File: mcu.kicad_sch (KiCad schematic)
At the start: 20 parts, among them J1 Conn_01x05, U1 STM32G473CCUx, Y1 8 MHz

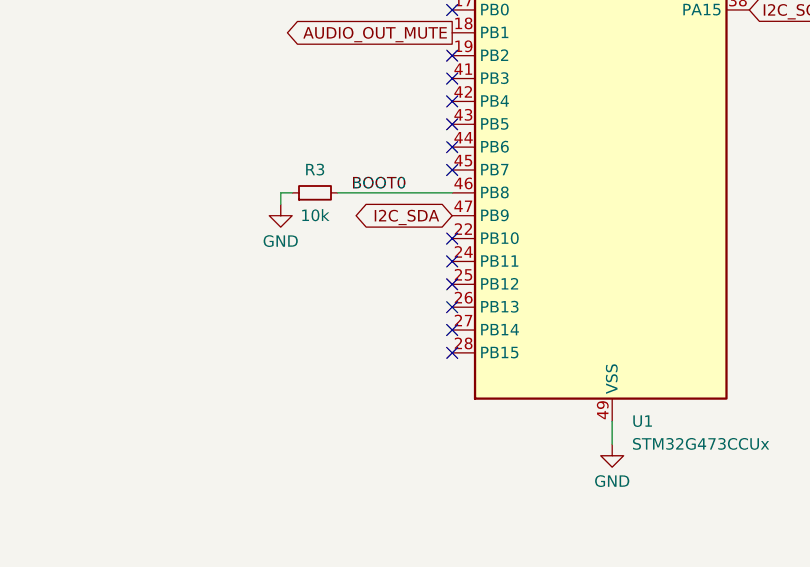
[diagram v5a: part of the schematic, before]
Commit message: J2 Corrected, More TP added.
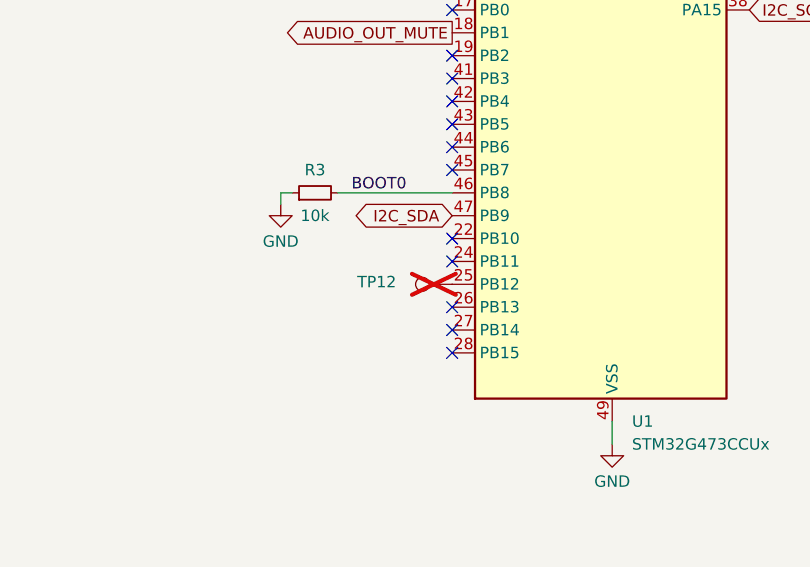
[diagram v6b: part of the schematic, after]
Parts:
- added TP12: GP, TestPoint:TestPoint_Pad_D1.0mm, symbol Connector:TestPoint
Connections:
- net at U1.25 (PB12): now also TP12.1
- no-connect marks 24 -> 23
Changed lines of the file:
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@@
+	)
+	(no_connect
+		(at 154.94 96.52)
+	)
+	(no_connect
+		(at 121.92 129.54)
+	)
+	(no_connect
+		(at 154.94 93.98)
+	)
+	(no_connect
+		(at 121.92 119.38)
+	)
+	(no_connect
+		(at 121.92 139.7)
+	)
+	(no_connect
+		(at 121.92 132.08)
+	)
+	(no_connect
+		(at 121.92 104.14)
+	)
+	(no_connect
+		(at 121.92 142.24)
+	)
+	(no_connect
+		(at 121.92 121.92)
+	)
+	(no_connect
+		(at 121.92 88.9)
+	)
+	(no_connect
+		(at 121.92 114.3)
+	)
+	(no_connect
+		(at 134.62 60.96)
+	)
+	(no_connect
+		(at 121.92 116.84)
+	)
+	(no_connect
+		(at 121.92 83.82)
+	)
+	(no_connect
+		(at 121.92 96.52)
 	)
 	(no_connect
 		(at 121.92 137.16)
-	)
-	(no_connect
-		(at 154.94 96.52)
-	)
-	(no_connect
-		(at 121.92 129.54)
-	)
-	(no_connect
-		(at 154.94 93.98)
-	)
-	(no_connect
-		(at 121.92 119.38)
-	)
-	(no_connect
-		(at 121.92 132.08)
-	)
-	(no_connect
-		(at 121.92 134.62)
-	)
-	(no_connect
-		(at 121.92 104.14)
-	)
-	(no_connect
-		(at 121.92 142.24)
-	)
-	(no_connect
-		(at 121.92 121.92)
-	)
-	(no_connect
-		(at 121.92 88.9)
-	)
-	(no_connect
-		(at 121.92 114.3)
-	)
-	(no_connect
-		(at 134.62 60.96)
-	)
-	(no_connect
-		(at 121.92 116.84)
-	)
-	(no_connect
-		(at 121.92 83.82)
-	)
-	(no_connect
-		(at 121.92 139.7)
-	)
-	(no_connect
-		(at 121.92 96.52)
 	)
 	(no_connect
@@
 					(unit 1)
 				)
+			)
+		)
+	)
+	(symbol
+		(lib_id "Connector:TestPoint")
+		(at 121.92 134.62 90)
+		(unit 1)
+		(exclude_from_sim no)
+		(in_bom no)
+		(on_board yes)
+		(dnp yes)
+		(property "Reference" "TP12"
+			(at 113.538 134.366 90)
+			(effects
+				(font
+					(size 1.27 1.27)
+				)
+			)
+		)
+		(property "Value" "GP"
+			(at 116.84 133.3501 90)
+			(effects
+				(font
+					(size 1.27 1.27)
+				)
+				(justify left)
+				(hide yes)
+			)
+		)
+		(property "Footprint" "TestPoint:TestPoint_Pad_D1.0mm"
+			(at 121.92 129.54 0)
+			(effects
+				(font
+					(size 1.27 1.27)
+				)
+				(hide yes)
+			)
+		)
+		(property "Datasheet" "~"
+			(at 121.92 129.54 0)
+			(effects
+				(font
+					(size 1.27 1.27)
+				)
+				(hide yes)
+			)
+		)
+		(property "Description" ""
+			(at 121.92 134.62 0)
+			(effects
+				(font
+					(size 1.27 1.27)
+				)
+				(hide yes)
+			)
+		)
+		(property "MPN" ""
+			(at 121.92 134.62 0)
+			(effects
+				(font
+					(size 1.27 1.27)
+				)
+				(hide yes)
+			)
+		)
+		(property "Height" ""
+			(at 121.92 134.62 0)
+			(effects
+				(font
+					(size 1.27 1.27)
+				)
+				(hide yes)
+			)
+		)
+		(property "Manufacturer_Name" ""
+			(at 121.92 134.62 0)
+			(effects
+				(font
+					(size 1.27 1.27)
+				)
+				(hide yes)
+			)
+		)
+		(property "Manufacturer_Part_Number" ""
+			(at 121.92 134.62 0)
+			(effects
+				(font
+					(size 1.27 1.27)
+				)
+				(hide yes)
+			)
+		)
+		(property "Mouser Part Number" ""
+			(at 121.92 134.62 0)
+			(effects
+				(font
+					(size 1.27 1.27)
+				)
+				(hide yes)
+			)
+		)
+		(property "Mouser Price/Stock" ""
+			(at 121.92 134.62 0)
+			(effects
+				(font
+					(size 1.27 1.27)
+				)
+				(hide yes)
+			)
+		)
+		(property "JLC" ""
+			(at 121.92 134.62 0)
+			(effects
+				(font
+					(size 1.27 1.27)
+				)
+				(hide yes)
+			)
+		)
+		(pin "1"
+		)
+		(instances
+			(project "micro17"
+				(path "/8b0d7f56-1962-40c9-8b95-6d4fe558acbc/9f9e0b5b-f07d-4ebd-b315-be375c62719d"
+					(reference "TP12")
+					(unit 1)
+				)

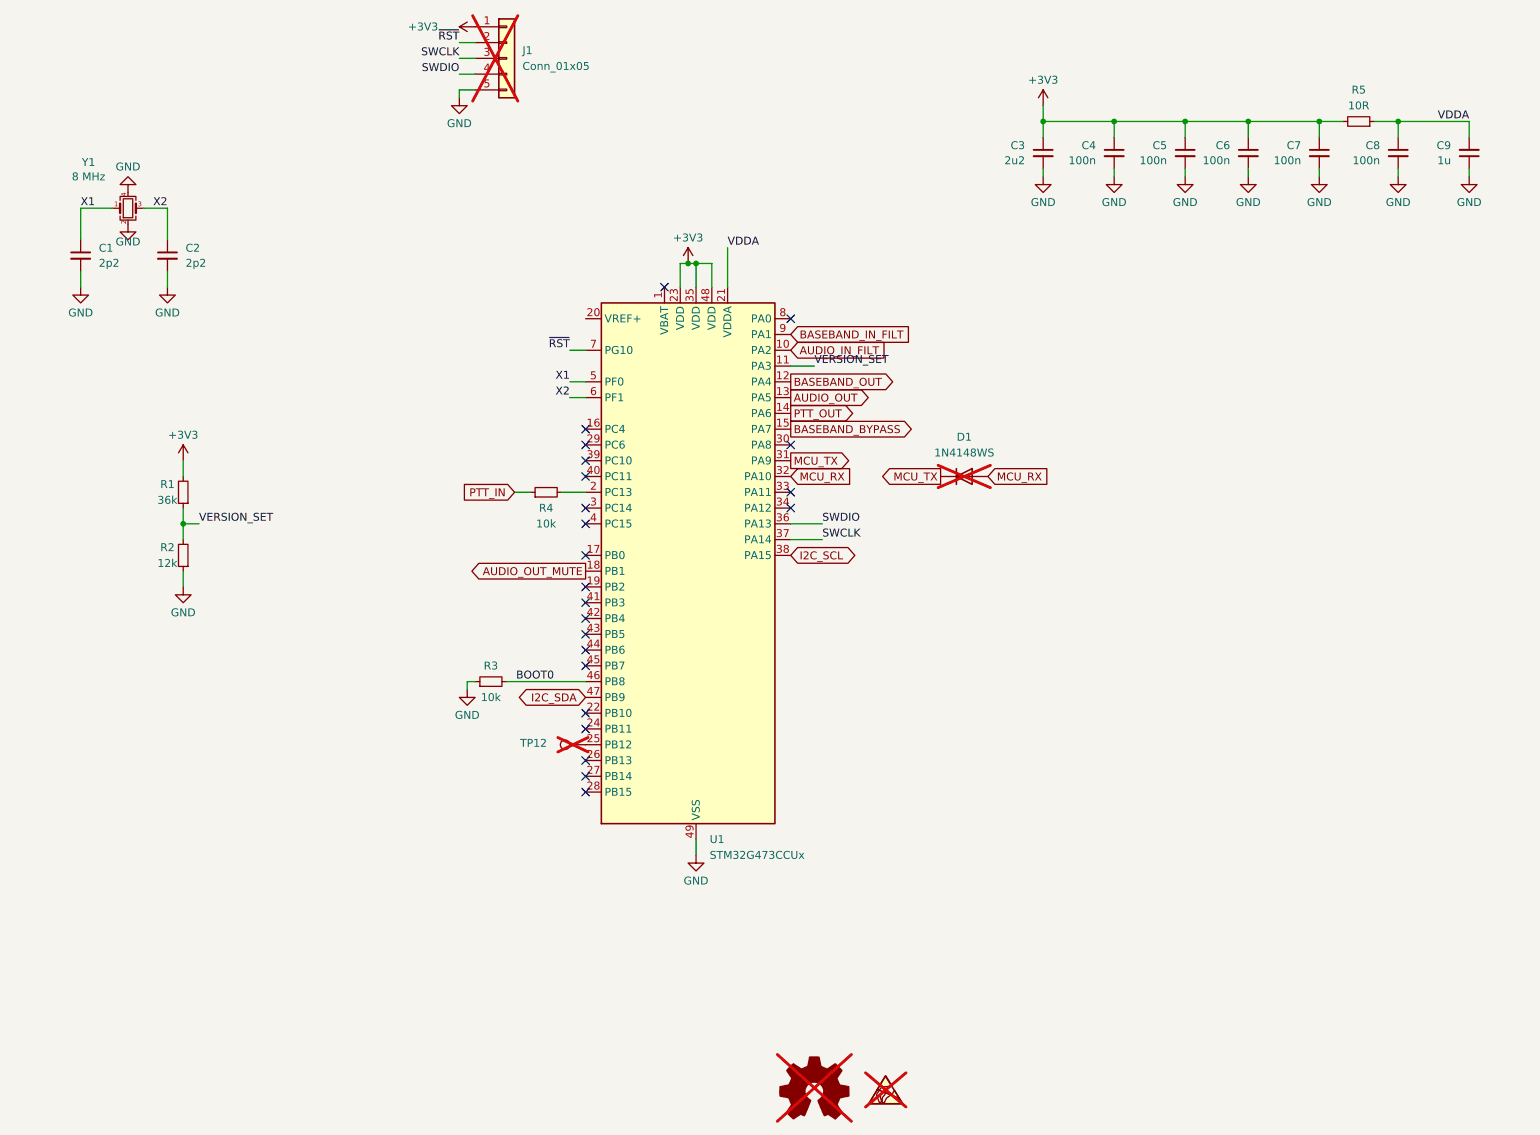
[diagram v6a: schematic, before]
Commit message: PA2 Bias add, USB conn add.
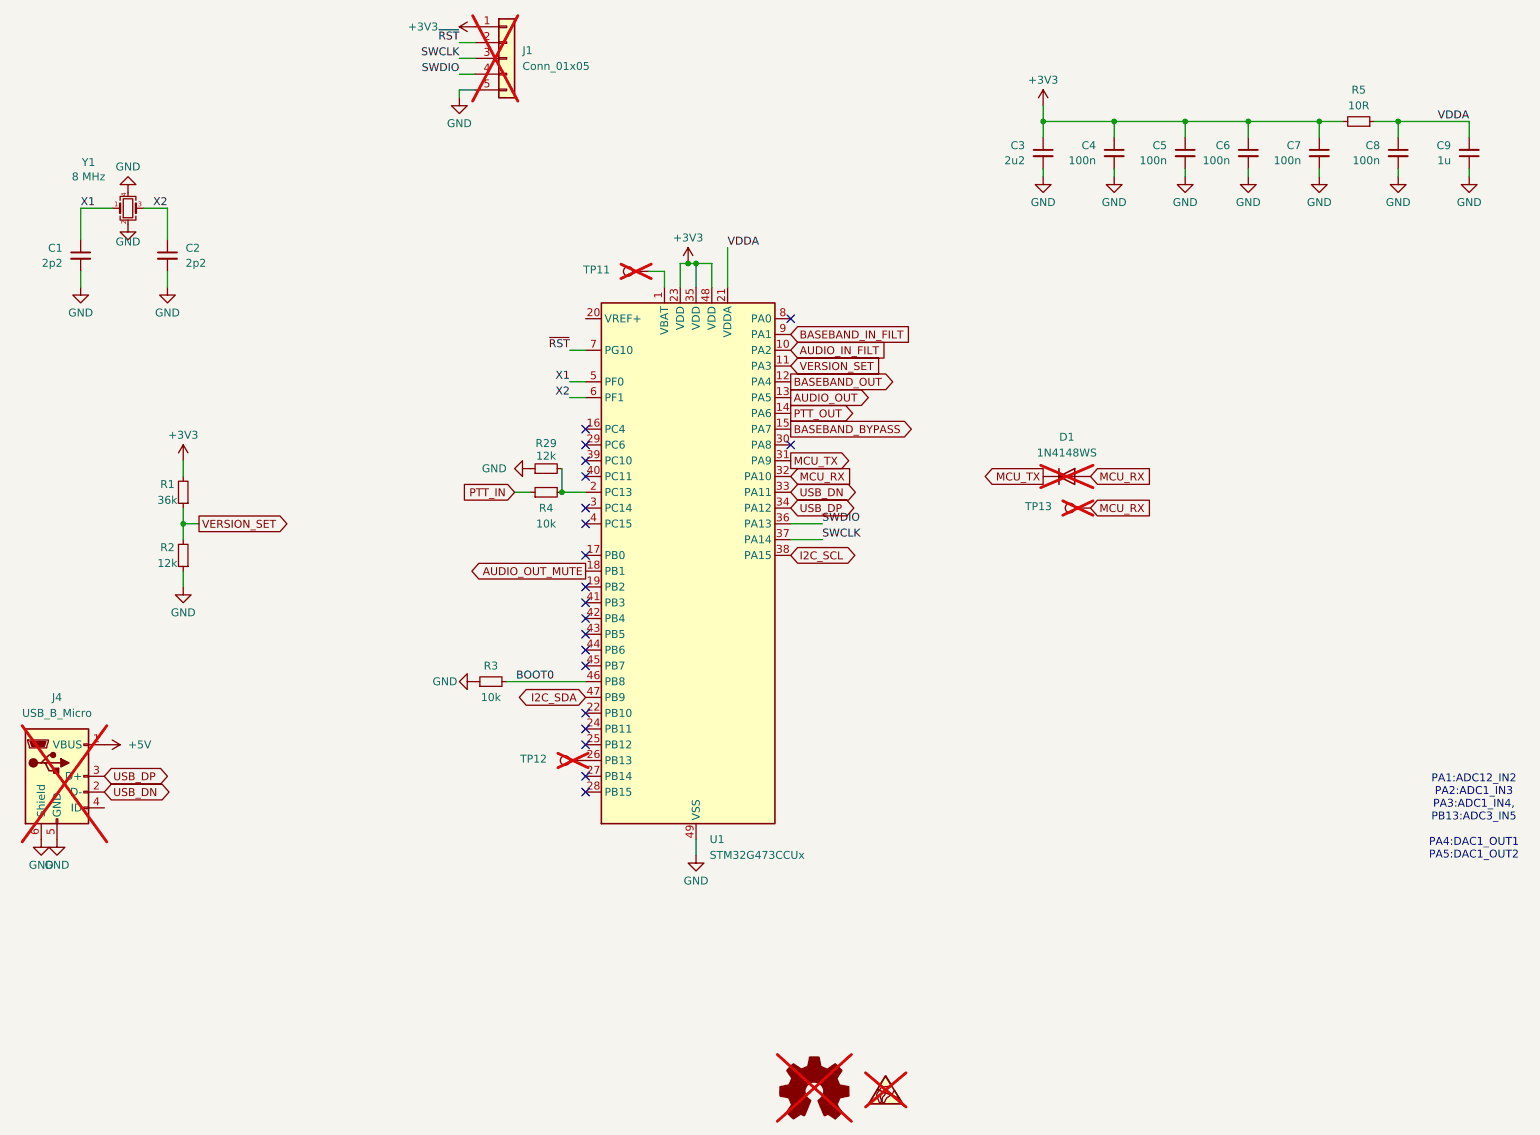
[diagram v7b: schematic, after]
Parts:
- added J4: USB_B_Micro, Connector_USB:USB_Micro-B_Molex_47346-0001, symbol Connector:USB_B_Micro
- added R29: 12k, Resistor_SMD:R_0402_1005Metric, symbol Device:R_Small
- added TP11, TP13: GP, TestPoint:TestPoint_Pad_D1.0mm, symbol Connector:TestPoint
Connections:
- net GND: now also J4.5 (GND), J4.6 (Shield), R29.1
- net MCU_RX: now also TP13.1
- net at TP12.1: now also U1.26 (PB13); no longer U1.25 (PB12)
- net at U1.1 (VBAT): now also TP11.1
- net at R4.2, U1.2 (PC13): now also R29.2
- net USB_DN: now reaches U1.33 (PA11)
- net USB_DN: now also J4.2 (D-)
- net USB_DP: now reaches U1.34 (PA12)
- net USB_DP: now also J4.3 (D+)
- new net +5V: J4.1 (VBUS)
- no-connect marks 23 -> 20
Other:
- note added: "PA1:ADC12_IN2 PA2:ADC1_IN3 PA3:ADC1_IN4, PB13:ADC3_IN5 PA4:DAC1_OUT1 PA5:DAC1_OUT2"
- title: Micro17 - OpenRTX on a Module -> Micro17 - OpenRTX on a Module for Icom Radios
- moved on the sheet: D1, TP12
